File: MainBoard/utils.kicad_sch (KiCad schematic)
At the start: 22 parts, among them J1 touch plate, J2 Matrix_in, Q1 AO3400A, Q2 AO3401A, Q3 PT1921C, Q4 PT1921C, U2 AT42QT1011-TSHR, U3 LIS3DH

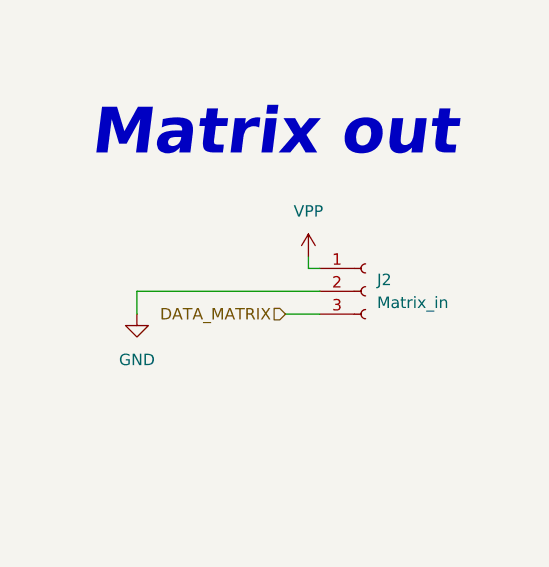
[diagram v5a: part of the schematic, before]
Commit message: Udpate project variables and add texts
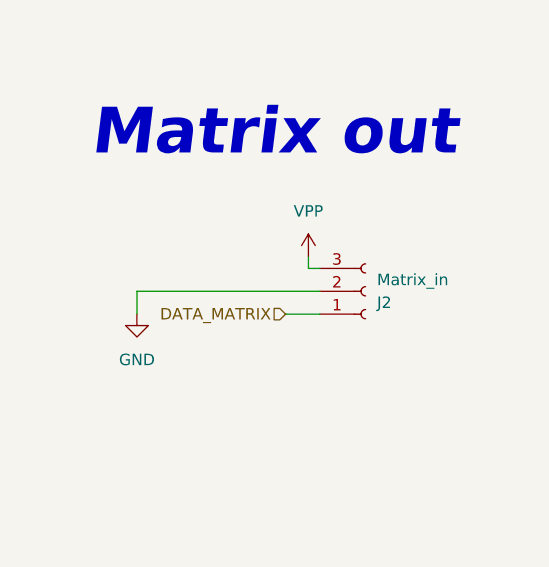
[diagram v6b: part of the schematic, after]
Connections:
- net DATA_MATRIX: now also J2.1 (Pin_1); no longer J2.3 (Pin_3)
- net VPP: now also J2.3 (Pin_3); no longer J2.1 (Pin_1)
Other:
- title: blob -> VirtualBlob
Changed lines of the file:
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@@
 	(paper "A4")
 	(title_block
-		(title "blob")
+		(title "VirtualBlob")
 		(date "2025-09-15")
-		(rev "3.2.0")
+		(rev "0.4.0")
 		(company "Miłosz Derżko")
 	)
@@
 		(lib_id "Connector:Conn_01x03_Socket")
 		(at 255.27 54.61 0)
+		(mirror x)
 		(unit 1)
 		(exclude_from_sim no)
@@
 		(on_board yes)
 		(dnp no)
-		(fields_autoplaced yes)
 		(property "Reference" "J2"
-			(at 256.54 53.3399 0)
+			(at 256.54 55.8801 0)
 			(effects
 				(font
@@
 		)
 		(property "Value" "Matrix_in"
-			(at 256.54 55.8799 0)
+			(at 256.54 53.3401 0)
 			(effects
 				(font

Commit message: Change naming of project
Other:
- company: Miłosz Derżko -> ${Company}
- title: VirtualBlob -> ${ProjectTitle}
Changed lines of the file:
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@@
 	(paper "A4")
 	(title_block
-		(title "VirtualBlob")
+		(title "${ProjectTitle}")
 		(date "2025-09-15")
-		(rev "0.4.0")
-		(company "Miłosz Derżko")
+		(rev "${Revision}")
+		(company "${Company}")
 	)
 	(text "OPTO"
@@
 		)
 		(instances
-			(project "mainboard"
+			(project "MainBoard"
 				(path "/9e709b97-b403-4027-b7d8-a3ed3b3557e2/49bfffe8-8446-437a-9339-1d6b2ed362e6"
 					(reference "R18")
@@
 		)
 		(instances
-			(project "mainboard"
+			(project "MainBoard"
 				(path "/9e709b97-b403-4027-b7d8-a3ed3b3557e2/49bfffe8-8446-437a-9339-1d6b2ed362e6"
 					(reference "#PWR041")
@@
 		)
 		(instances
-			(project "mainboard"
+			(project "MainBoard"
 				(path "/9e709b97-b403-4027-b7d8-a3ed3b3557e2/49bfffe8-8446-437a-9339-1d6b2ed362e6"
 					(reference "#PWR06")
@@
 		)
 		(instances
-			(project "mainboard"
+			(project "MainBoard"
 				(path "/9e709b97-b403-4027-b7d8-a3ed3b3557e2/49bfffe8-8446-437a-9339-1d6b2ed362e6"
 					(reference "#PWR044")
@@
 		)
 		(instances
-			(project "mainboard"
+			(project "MainBoard"
 				(path "/9e709b97-b403-4027-b7d8-a3ed3b3557e2/49bfffe8-8446-437a-9339-1d6b2ed362e6"
 					(reference "C15")
@@
 		)
 		(instances
-			(project "mainboard"
+			(project "MainBoard"
 				(path "/9e709b97-b403-4027-b7d8-a3ed3b3557e2/49bfffe8-8446-437a-9339-1d6b2ed362e6"
 					(reference "#PWR034")
@@
 		)
 		(instances
-			(project "mainboard"
+			(project "MainBoard"
 				(path "/9e709b97-b403-4027-b7d8-a3ed3b3557e2/49bfffe8-8446-437a-9339-1d6b2ed362e6"
 					(reference "C16")
@@
 		)
 		(instances
-			(project "mainboard"
+			(project "MainBoard"
 				(path "/9e709b97-b403-4027-b7d8-a3ed3b3557e2/49bfffe8-8446-437a-9339-1d6b2ed362e6"
 					(reference "Q4")
@@
 		)
 		(instances
-			(project "mainboard"
+			(project "MainBoard"
 				(path "/9e709b97-b403-4027-b7d8-a3ed3b3557e2/49bfffe8-8446-437a-9339-1d6b2ed362e6"
 					(reference "#PWR032")
@@
 		)
 		(instances
-			(project "mainboard"
+			(project "MainBoard"
 				(path "/9e709b97-b403-4027-b7d8-a3ed3b3557e2/49bfffe8-8446-437a-9339-1d6b2ed362e6"
 					(reference "R4")
@@
 		)
 		(instances
-			(project "mainboard"
+			(project "MainBoard"
 				(path "/9e709b97-b403-4027-b7d8-a3ed3b3557e2/49bfffe8-8446-437a-9339-1d6b2ed362e6"
 					(reference "#PWR01")
@@
 		)
 		(instances
-			(project "mainboard"
+			(project "MainBoard"
 				(path "/9e709b97-b403-4027-b7d8-a3ed3b3557e2/49bfffe8-8446-437a-9339-1d6b2ed362e6"
 					(reference "#PWR053")
@@
 		)
 		(instances
-			(project "mainboard"
+			(project "MainBoard"
 				(path "/9e709b97-b403-4027-b7d8-a3ed3b3557e2/49bfffe8-8446-437a-9339-1d6b2ed362e6"
 					(reference "R5")
@@
 		)
 		(instances
-			(project "mainboard"
+			(project "MainBoard"
 				(path "/9e709b97-b403-4027-b7d8-a3ed3b3557e2/49bfffe8-8446-437a-9339-1d6b2ed362e6"
 					(reference "#PWR035")
@@
 		)
 		(instances
-			(project "mainboard"
+			(project "MainBoard"
 				(path "/9e709b97-b403-4027-b7d8-a3ed3b3557e2/49bfffe8-8446-437a-9339-1d6b2ed362e6"
 					(reference "#PWR025")
@@
 		)
 		(instances
-			(project "mainboard"
+			(project "MainBoard"
 				(path "/9e709b97-b403-4027-b7d8-a3ed3b3557e2/49bfffe8-8446-437a-9339-1d6b2ed362e6"
 					(reference "C14")
@@
 		)
 		(instances
-			(project "mainboard"
+			(project "MainBoard"
 				(path "/9e709b97-b403-4027-b7d8-a3ed3b3557e2/49bfffe8-8446-437a-9339-1d6b2ed362e6"
 					(reference "R8")
@@
 		)
 		(instances
-			(project "mainboard"
+			(project "MainBoard"
 				(path "/9e709b97-b403-4027-b7d8-a3ed3b3557e2/49bfffe8-8446-437a-9339-1d6b2ed362e6"
 					(reference "#PWR054")
@@
 		)
 		(instances
-			(project "mainboard"
+			(project "MainBoard"
 				(path "/9e709b97-b403-4027-b7d8-a3ed3b3557e2/49bfffe8-8446-437a-9339-1d6b2ed362e6"
 					(reference "#PWR033")
@@
 		)
 		(instances
-			(project "mainboard"
+			(project "MainBoard"
 				(path "/9e709b97-b403-4027-b7d8-a3ed3b3557e2/49bfffe8-8446-437a-9339-1d6b2ed362e6"
 					(reference "#PWR027")
@@
 		)
 		(instances
-			(project "mainboard"
+			(project "MainBoard"
 				(path "/9e709b97-b403-4027-b7d8-a3ed3b3557e2/49bfffe8-8446-437a-9339-1d6b2ed362e6"
 					(reference "R17")
@@
 		)
 		(instances
-			(project "mainboard"
+			(project "MainBoard"
 				(path "/9e709b97-b403-4027-b7d8-a3ed3b3557e2/49bfffe8-8446-437a-9339-1d6b2ed362e6"
 					(reference "#PWR024")
@@
 		)
 		(instances
-			(project "mainboard"
+			(project "MainBoard"
 				(path "/9e709b97-b403-4027-b7d8-a3ed3b3557e2/49bfffe8-8446-437a-9339-1d6b2ed362e6"
 					(reference "#PWR060")
@@
 		)
 		(instances
-			(project "mainboard"
+			(project "MainBoard"
 				(path "/9e709b97-b403-4027-b7d8-a3ed3b3557e2/49bfffe8-8446-437a-9339-1d6b2ed362e6"
 					(reference "#PWR028")
@@
 		)
 		(instances
-			(project "mainboard"
+			(project "MainBoard"
 				(path "/9e709b97-b403-4027-b7d8-a3ed3b3557e2/49bfffe8-8446-437a-9339-1d6b2ed362e6"
 					(reference "R10")
@@
 		)
 		(instances
-			(project "mainboard"
+			(project "MainBoard"
 				(path "/9e709b97-b403-4027-b7d8-a3ed3b3557e2/49bfffe8-8446-437a-9339-1d6b2ed362e6"
 					(reference "C17")
@@
 		)
 		(instances
-			(project "mainboard"
+			(project "MainBoard"
 				(path "/9e709b97-b403-4027-b7d8-a3ed3b3557e2/49bfffe8-8446-437a-9339-1d6b2ed362e6"
 					(reference "#PWR031")
@@
 		)
 		(instances
-			(project "mainboard"
+			(project "MainBoard"
 				(path "/9e709b97-b403-4027-b7d8-a3ed3b3557e2/49bfffe8-8446-437a-9339-1d6b2ed362e6"
 					(reference "#PWR03")
@@
 		)
 		(instances
-			(project "mainboard"
+			(project "MainBoard"
 				(path "/9e709b97-b403-4027-b7d8-a3ed3b3557e2/49bfffe8-8446-437a-9339-1d6b2ed362e6"
 					(reference "U3")
@@
 		)
 		(instances
-			(project "mainboard"
+			(project "MainBoard"
 				(path "/9e709b97-b403-4027-b7d8-a3ed3b3557e2/49bfffe8-8446-437a-9339-1d6b2ed362e6"
 					(reference "#PWR042")
@@
 		)
 		(instances
-			(project "mainboard"
+			(project "MainBoard"
 				(path "/9e709b97-b403-4027-b7d8-a3ed3b3557e2/49bfffe8-8446-437a-9339-1d6b2ed362e6"
 					(reference "#PWR037")
@@
 		)
 		(instances
-			(project "mainboard"
+			(project "MainBoard"
 				(path "/9e709b97-b403-4027-b7d8-a3ed3b3557e2/49bfffe8-8446-437a-9339-1d6b2ed362e6"
 					(reference "R11")
@@
 		)
 		(instances
-			(project "mainboard"
+			(project "MainBoard"
 				(path "/9e709b97-b403-4027-b7d8-a3ed3b3557e2/49bfffe8-8446-437a-9339-1d6b2ed362e6"
 					(reference "R12")
@@
 		)
 		(instances
-			(project "mainboard"
+			(project "MainBoard"
 				(path "/9e709b97-b403-4027-b7d8-a3ed3b3557e2/49bfffe8-8446-437a-9339-1d6b2ed362e6"
 					(reference "#PWR043")
@@
 		)
 		(instances
-			(project "mainboard"
+			(project "MainBoard"
 				(path "/9e709b97-b403-4027-b7d8-a3ed3b3557e2/49bfffe8-8446-437a-9339-1d6b2ed362e6"
 					(reference "J2")
@@
 		)
 		(instances
-			(project "mainboard"
+			(project "MainBoard"
 				(path "/9e709b97-b403-4027-b7d8-a3ed3b3557e2/49bfffe8-8446-437a-9339-1d6b2ed362e6"
 					(reference "#PWR05")
@@
 		)
 		(instances
-			(project "mainboard"
+			(project "MainBoard"
 				(path "/9e709b97-b403-4027-b7d8-a3ed3b3557e2/49bfffe8-8446-437a-9339-1d6b2ed362e6"
 					(reference "#PWR038")
@@
 		)
 		(instances
-			(project "mainboard"
+			(project "MainBoard"
 				(path "/9e709b97-b403-4027-b7d8-a3ed3b3557e2/49bfffe8-8446-437a-9339-1d6b2ed362e6"
 					(reference "#PWR062")
@@
 		)
 		(instances
-			(project "mainboard"
+			(project "MainBoard"
 				(path "/9e709b97-b403-4027-b7d8-a3ed3b3557e2/49bfffe8-8446-437a-9339-1d6b2ed362e6"
 					(reference "R6")

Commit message: add new spring touch
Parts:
- removed J1: touch plate, touch:FW-UU_05_11_28, symbol Connector:Conn_01x01_Pin
- added J3: Conn_01x02_Pin, touch:FW-UU_04_08_15, symbol Connector:Conn_01x02_Pin
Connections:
- net at R17.2: now also J3.1 (Pin_1)
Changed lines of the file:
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@@
+	)
+	(symbol
+		(lib_id "Connector:Conn_01x02_Pin")
+		(at 123.19 170.18 0)
+		(mirror y)
+		(unit 1)
+		(exclude_from_sim no)
+		(in_bom yes)
+		(on_board yes)
+		(dnp no)
+		(fields_autoplaced yes)
+		(property "Reference" "J3"
+			(at 124.46 170.1799 0)
+			(effects
+				(font
+					(size 1.27 1.27)
+				)
+				(justify right)
+			)
+		)
+		(property "Value" "Conn_01x02_Pin"
+			(at 124.46 172.7199 0)
+			(effects
+				(font
+					(size 1.27 1.27)
+				)
+				(justify right)
+			)
+		)
+		(property "Footprint" "touch:FW-UU_04_08_15"
+			(at 123.19 170.18 0)
+			(effects
+				(font
+					(size 1.27 1.27)
+				)
+				(hide yes)
+			)
+		)
+		(property "Datasheet" "~"
+			(at 123.19 170.18 0)
+			(effects
+				(font
+					(size 1.27 1.27)
+				)
+				(hide yes)
+			)
+		)
+		(property "Description" "Generic connector, single row, 01x02, script generated"
+			(at 123.19 170.18 0)
+			(effects
+				(font
+					(size 1.27 1.27)
+				)
+				(hide yes)
+			)
+		)
+		(pin "1"
+		)
+		(pin "2"
+		)
+		(instances
+			(project ""
+				(path "/9e709b97-b403-4027-b7d8-a3ed3b3557e2/49bfffe8-8446-437a-9339-1d6b2ed362e6"
+					(reference "J3")
+					(unit 1)
+				)
+			)
+		)
 	)
 	(symbol
@@
 					(unit 1)
 				)
-			)
-		)
-	)
-	(symbol
-		(lib_id "Connector:Conn_01x01_Pin")
-		(at 123.19 170.18 180)
-		(unit 1)
-		(exclude_from_sim no)
-		(in_bom yes)
-		(on_board yes)
-		(dnp no)
-		(fields_autoplaced yes)
-		(property "Reference" "J1"
-			(at 122.555 165.1 0)
-			(effects
-				(font
-					(size 1.27 1.27)
-				)
-			)
-		)
-		(property "Value" "touch plate"
-			(at 122.555 167.64 0)
-			(effects
-				(font
-					(size 1.27 1.27)
-				)
-			)
-		)
-		(property "Footprint" "touch:FW-UU_05_11_28"
-			(at 123.19 170.18 0)
-			(effects
-				(font
-					(size 1.27 1.27)
-				)
-				(hide yes)
-			)
-		)
-		(property "Datasheet" "~"
-			(at 123.19 170.18 0)
-			(effects
-				(font
-					(size 1.27 1.27)
-				)
-				(hide yes)
-			)
-		)
-		(property "Description" "Generic connector, single row, 01x01, script generated"
-			(at 123.19 170.18 0)
-			(effects
-				(font
-					(size 1.27 1.27)
-				)
-				(hide yes)
-			)
-		)
-		(pin "1"
-		)
-		(instances
-			(project ""
-				(path "/9e709b97-b403-4027-b7d8-a3ed3b3557e2/49bfffe8-8446-437a-9339-1d6b2ed362e6"
-					(reference "J1")
-					(unit 1)
-				)
